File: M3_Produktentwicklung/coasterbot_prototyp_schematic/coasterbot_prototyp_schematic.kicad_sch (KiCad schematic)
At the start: 22 parts, among them SW1 Main Switch, U10 FrontRight, U11 Front, U13 Aufnahme Coaster, U14 Ausschub Coaster, U2 Raspi Pico2 Controller Board, U3 Left, U4 Right, U5 FrontLeft, U6 BackLeft, U7 FrontRight, U8 BackRight, U9 FrontLeft

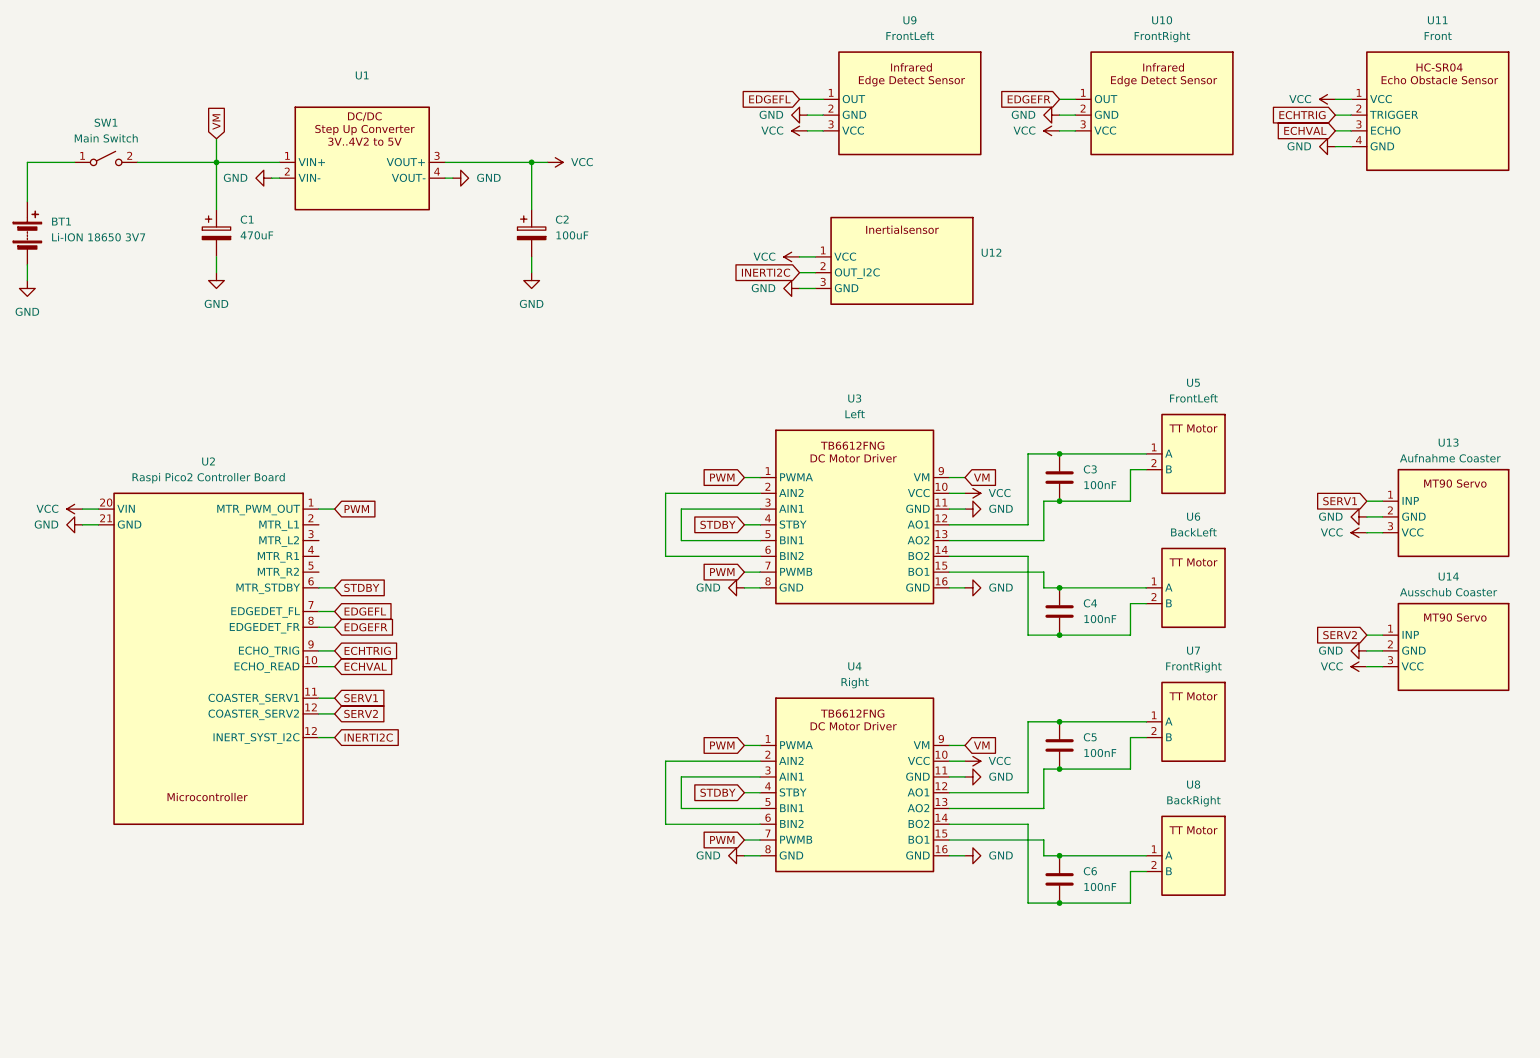
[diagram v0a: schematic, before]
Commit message: RGB LED und Taster für user mode toggle hinzugefuegt.
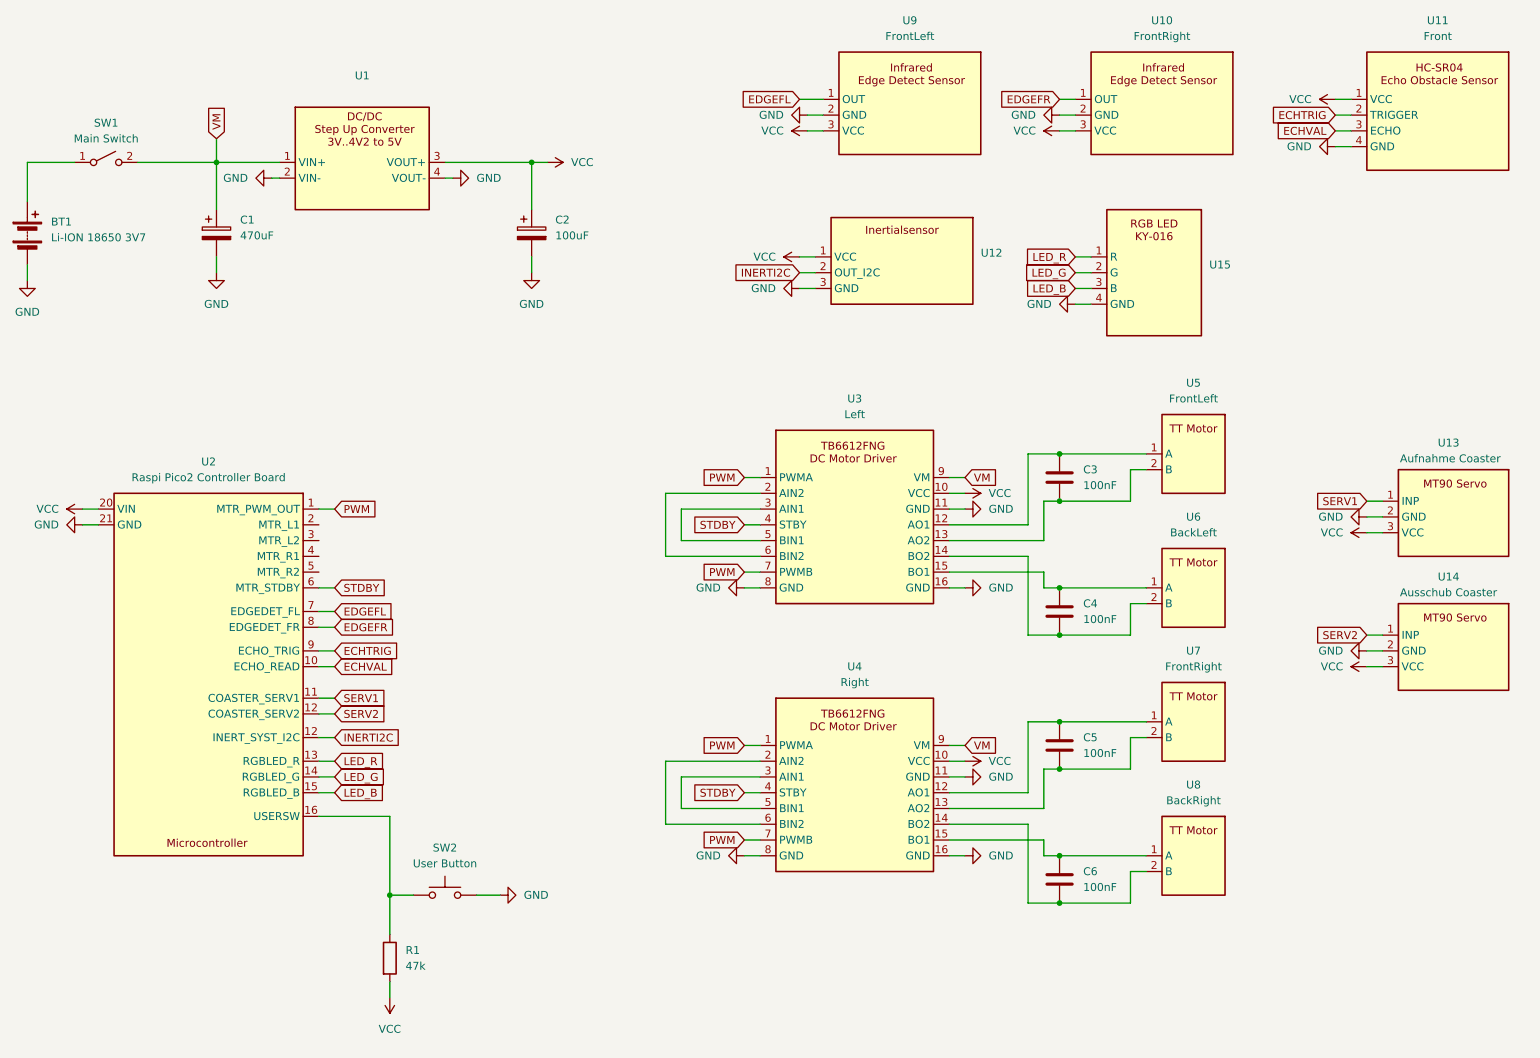
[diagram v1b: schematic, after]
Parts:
- added R1: 47k, symbol Device:R
- added SW2: User Button, symbol Switch:SW_Push
- added U15: ~, symbol components:RGBLed
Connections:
- net GND: now also SW2.2, U15.4 (GND)
- net VCC: now also R1.2
- new net: R1.1, SW2.1, U2.16 (USERSW)
- new net LED_B: U15.3 (B), U2.15 (RGBLED_B)
- new net LED_G: U15.2 (G), U2.14 (RGBLED_G)
- new net LED_R: U15.1 (R), U2.13 (RGBLED_R)

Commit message: 3V3 rail added, button pulls up from there.
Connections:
- net VCC: no longer R1.2
- new net +3.3V: R1.2, U2.22 (3V3)
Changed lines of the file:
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@@
 	(wire
 		(pts
+			(xy 33.02 100.33) (xy 35.56 100.33)
+		)
+		(stroke
+			(width 0)
+			(type default)
+		)
+	)
+	(wire
+		(pts
 			(xy 71.12 135.89) (xy 73.66 135.89)
 		)
@@
 	(wire
 		(pts
-			(xy 82.55 171.45) (xy 82.55 173.99)
+			(xy 82.55 171.45) (xy 82.55 175.26)
 		)
 		(stroke
@@
 	)
 	(symbol
+		(lib_id "power:+3.3V")
+		(at 33.02 100.33 90)
+		(unit 1)
+		(exclude_from_sim no)
+		(in_bom yes)
+		(on_board yes)
+		(dnp no)
+		(fields_autoplaced yes)
+		(property "Reference" "#PWR032"
+			(at 36.83 100.33 0)
+			(effects
+				(font
+					(size 1.27 1.27)
+				)
+				(hide yes)
+			)
+		)
+		(property "Value" "+3.3V"
+			(at 29.21 100.3299 90)
+			(effects
+				(font
+					(size 1.27 1.27)
+				)
+				(justify left)
+			)
+		)
+		(property "Footprint" ""
+			(at 33.02 100.33 0)
+			(effects
+				(font
+					(size 1.27 1.27)
+				)
+				(hide yes)
+			)
+		)
+		(property "Datasheet" ""
+			(at 33.02 100.33 0)
+			(effects
+				(font
+					(size 1.27 1.27)
+				)
+				(hide yes)
+			)
+		)
+		(property "Description" "Power symbol creates a global label with name \"+3.3V\""
+			(at 33.02 100.33 0)
+			(effects
+				(font
+					(size 1.27 1.27)
+				)
+				(hide yes)
+			)
+		)
+		(pin "1"
+		)
+		(instances
+			(project "coasterbot_prototyp_schematic"
+				(path "/eaf3b5d0-071d-4d14-8ed8-2bfc6560b869"
+					(reference "#PWR032")
+					(unit 1)
+				)
+			)
+		)
+	)
+	(symbol
 		(lib_id "power:VCC")
 		(at 149.86 34.29 90)
@@
 	(symbol
 		(lib_id "power:VCC")
-		(at 82.55 173.99 180)
-		(unit 1)
-		(exclude_from_sim no)
-		(in_bom yes)
-		(on_board yes)
-		(dnp no)
-		(fields_autoplaced yes)
-		(property "Reference" "#PWR030"
-			(at 82.55 170.18 0)
-			(effects
-				(font
-					(size 1.27 1.27)
-				)
-				(hide yes)
-			)
-		)
-		(property "Value" "VCC"
-			(at 82.55 179.07 0)
-			(effects
-				(font
-					(size 1.27 1.27)
-				)
-			)
-		)
-		(property "Footprint" ""
-			(at 82.55 173.99 0)
-			(effects
-				(font
-					(size 1.27 1.27)
-				)
-				(hide yes)
-			)
-		)
-		(property "Datasheet" ""
-			(at 82.55 173.99 0)
-			(effects
-				(font
-					(size 1.27 1.27)
-				)
-				(hide yes)
-			)
-		)
-		(property "Description" "Power symbol creates a global label with name \"VCC\""
-			(at 82.55 173.99 0)
-			(effects
-				(font
-					(size 1.27 1.27)
-				)
-				(hide yes)
-			)
-		)
-		(pin "1"
-		)
-		(instances
-			(project "coasterbot_prototyp_schematic"
-				(path "/eaf3b5d0-071d-4d14-8ed8-2bfc6560b869"
-					(reference "#PWR030")
-					(unit 1)
-				)
-			)
-		)
-	)
-	(symbol
-		(lib_id "power:VCC")
 		(at 234.95 29.21 90)
 		(unit 1)
@@
 		(pin "16"
 		)
+		(pin "22"
+		)
 		(instances
 			(project "coasterbot_prototyp_schematic"
@@
 					(unit 1)
 				)
+			)
+		)
+	)
+	(symbol
+		(lib_id "power:+3.3V")
+		(at 82.55 175.26 180)
+		(unit 1)
+		(exclude_from_sim no)
+		(in_bom yes)
+		(on_board yes)
+		(dnp no)
+		(fields_autoplaced yes)
+		(property "Reference" "#PWR033"
+			(at 82.55 171.45 0)
+			(effects
+				(font
+					(size 1.27 1.27)
+				)
+				(hide yes)
+			)
+		)
+		(property "Value" "+3.3V"
+			(at 82.55 180.34 0)
+			(effects
+				(font
+					(size 1.27 1.27)
+				)
+			)
+		)
+		(property "Footprint" ""
+			(at 82.55 175.26 0)
+			(effects
+				(font
+					(size 1.27 1.27)
+				)
+				(hide yes)
+			)
+		)
+		(property "Datasheet" ""
+			(at 82.55 175.26 0)
+			(effects
+				(font
+					(size 1.27 1.27)
+				)
+				(hide yes)
+			)
+		)
+		(property "Description" "Power symbol creates a global label with name \"+3.3V\""
+			(at 82.55 175.26 0)
+			(effects
+				(font
+					(size 1.27 1.27)
+				)
+				(hide yes)
+			)
+		)
+		(pin "1"
+		)
+		(instances
+			(project "coasterbot_prototyp_schematic"
+				(path "/eaf3b5d0-071d-4d14-8ed8-2bfc6560b869"
+					(reference "#PWR033")
+					(unit 1)
+				)

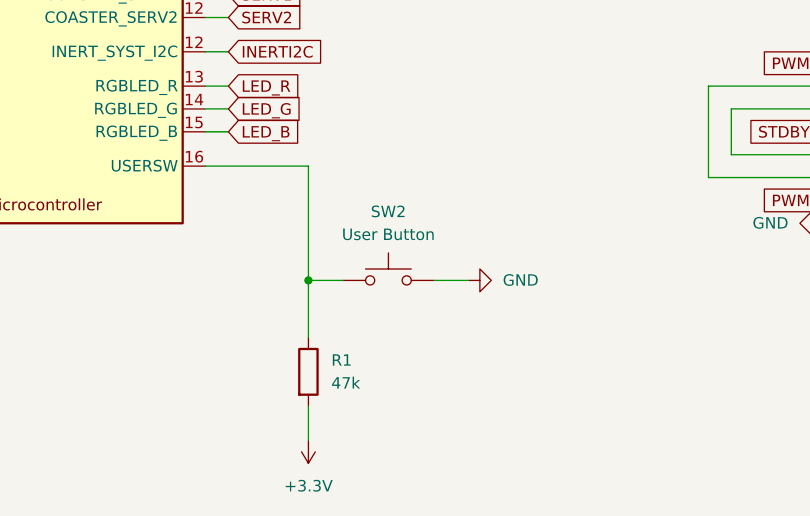
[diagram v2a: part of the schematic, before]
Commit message: Taster entprellung
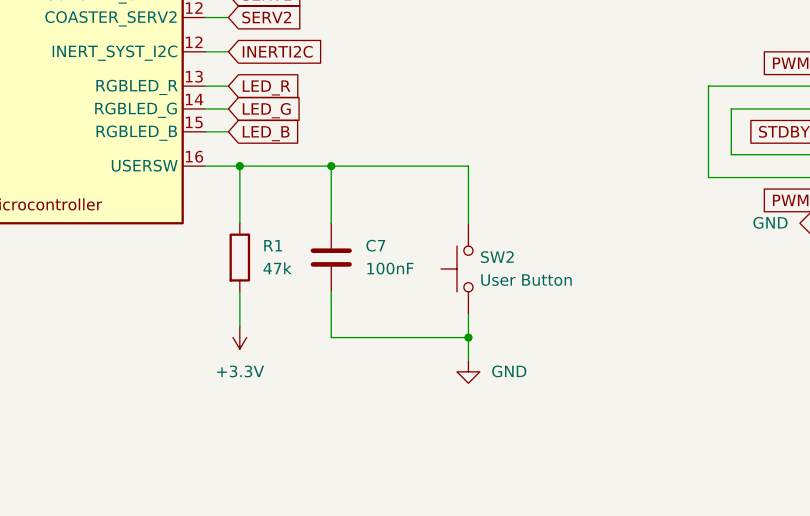
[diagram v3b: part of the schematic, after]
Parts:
- added C7: 100nF, symbol Device:C
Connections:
- net GND: now also SW2.1, C7.2; no longer SW2.2
- net at R1.1, U2.16 (USERSW): now also SW2.2, C7.1; no longer SW2.1
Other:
- moved on the sheet: R1, SW2

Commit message: fehlende Verbindung Microcontroller zu Motor Regler gefixt.
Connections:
- net at U3.2 (AIN2), U3.6 (BIN2): now also U2.3 (MTR_L2)
- net at U3.3 (AIN1), U3.5 (BIN1): now also U2.2 (MTR_L1)
- net at U2.4 (MTR_R1): now also U4.3 (AIN1), U4.5 (BIN1)
- net at U2.5 (MTR_R2): now also U4.2 (AIN2), U4.6 (BIN2)
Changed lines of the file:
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@@
+	)
+	(junction
+		(at 129.54 140.97)
+		(diameter 0)
+		(color 0 0 0 0)
 	)
 	(junction
@@
 	)
 	(junction
+		(at 127 100.33)
+		(diameter 0)
+		(color 0 0 0 0)
+	)
+	(junction
 		(at 190.5 158.75)
 		(diameter 0)
@@
 	)
 	(junction
+		(at 129.54 97.79)
+		(diameter 0)
+		(color 0 0 0 0)
+	)
+	(junction
 		(at 85.09 144.78)
+		(diameter 0)
+		(color 0 0 0 0)
+	)
+	(junction
+		(at 127 143.51)
 		(diameter 0)
 		(color 0 0 0 0)
@@
 	(wire
 		(pts
+			(xy 115.57 143.51) (xy 127 143.51)
+		)
+		(stroke
+			(width 0)
+			(type default)
+		)
+	)
+	(wire
+		(pts
 			(xy 142.24 138.43) (xy 129.54 138.43)
 		)
@@
 	(wire
 		(pts
+			(xy 127 100.33) (xy 127 102.87)
+		)
+		(stroke
+			(width 0)
+			(type default)
+		)
+	)
+	(wire
+		(pts
 			(xy 240.03 93.98) (xy 242.57 93.98)
 		)
@@
 	(wire
 		(pts
+			(xy 71.12 100.33) (xy 127 100.33)
+		)
+		(stroke
+			(width 0)
+			(type default)
+		)
+	)
+	(wire
+		(pts
 			(xy 204.47 132.08) (xy 201.93 132.08)
 		)
@@
 	(wire
 		(pts
+			(xy 71.12 102.87) (xy 118.11 102.87)
+		)
+		(stroke
+			(width 0)
+			(type default)
+		)
+	)
+	(wire
+		(pts
+			(xy 127 135.89) (xy 127 143.51)
+		)
+		(stroke
+			(width 0)
+			(type default)
+		)
+	)
+	(wire
+		(pts
 			(xy 24.13 39.37) (xy 31.75 39.37)
 		)
@@
 	(wire
 		(pts
-			(xy 127 92.71) (xy 127 102.87)
+			(xy 127 92.71) (xy 127 100.33)
 		)
 		(stroke
@@
 	(wire
 		(pts
-			(xy 129.54 138.43) (xy 129.54 143.51)
+			(xy 129.54 138.43) (xy 129.54 140.97)
 		)
 		(stroke
@@
 	(wire
 		(pts
+			(xy 118.11 102.87) (xy 118.11 140.97)
+		)
+		(stroke
+			(width 0)
+			(type default)
+		)
+	)
+	(wire
+		(pts
 			(xy 172.72 146.05) (xy 185.42 146.05)
 		)
@@
 	(wire
 		(pts
+			(xy 115.57 105.41) (xy 115.57 143.51)
+		)
+		(stroke
+			(width 0)
+			(type default)
+		)
+	)
+	(wire
+		(pts
 			(xy 190.5 31.75) (xy 193.04 31.75)
 		)
@@
 	(wire
 		(pts
+			(xy 129.54 97.79) (xy 129.54 100.33)
+		)
+		(stroke
+			(width 0)
+			(type default)
+		)
+	)
+	(wire
+		(pts
 			(xy 240.03 99.06) (xy 242.57 99.06)
 		)
@@
 	(wire
 		(pts
+			(xy 118.11 140.97) (xy 129.54 140.97)
+		)
+		(stroke
+			(width 0)
+			(type default)
+		)
+	)
+	(wire
+		(pts
 			(xy 172.72 138.43) (xy 175.26 138.43)
 		)
@@
 	(wire
 		(pts
+			(xy 127 143.51) (xy 127 146.05)
+		)
+		(stroke
+			(width 0)
+			(type default)
+		)
+	)
+	(wire
+		(pts
 			(xy 187.96 107.95) (xy 190.5 107.95)
 		)
@@
 	(wire
 		(pts
-			(xy 129.54 95.25) (xy 129.54 100.33)
+			(xy 129.54 95.25) (xy 129.54 97.79)
 		)
 		(stroke
@@
 	(wire
 		(pts
-			(xy 127 135.89) (xy 127 146.05)
-		)
-		(stroke
-			(width 0)
-			(type default)
-		)
-	)
-	(wire
-		(pts
 			(xy 193.04 54.61) (xy 195.58 54.61)
 		)
@@
 	(wire
 		(pts
+			(xy 129.54 140.97) (xy 129.54 143.51)
+		)
+		(stroke
+			(width 0)
+			(type default)
+		)
+	)
+	(wire
+		(pts
 			(xy 190.5 158.75) (xy 201.93 158.75)
 		)
@@
 	(wire
 		(pts
+			(xy 71.12 105.41) (xy 115.57 105.41)
+		)
+		(stroke
+			(width 0)
+			(type default)
+		)
+	)
+	(wire
+		(pts
 			(xy 139.7 90.17) (xy 142.24 90.17)
 		)
@@
 		)
 		(stroke
+			(width 0)
+			(type default)
+		)
+	)
+	(wire
+		(pts
+			(xy 71.12 97.79) (xy 129.54 97.79)
+		)
+		(stroke
